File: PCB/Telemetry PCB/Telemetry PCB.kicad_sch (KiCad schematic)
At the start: 48 parts, among them IC1 E22-900M22S, J1 USB_C_Receptacle_USB2.0_16P, J2 Batt, J3 Serial Debug Header 1x4, J4 GPS, J5 Conn_01x04_Pin, SW1 SW_MEC_5E, SW2 SW_MEC_5E, U1 AP62200WU, U2 STM32F411CEUx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

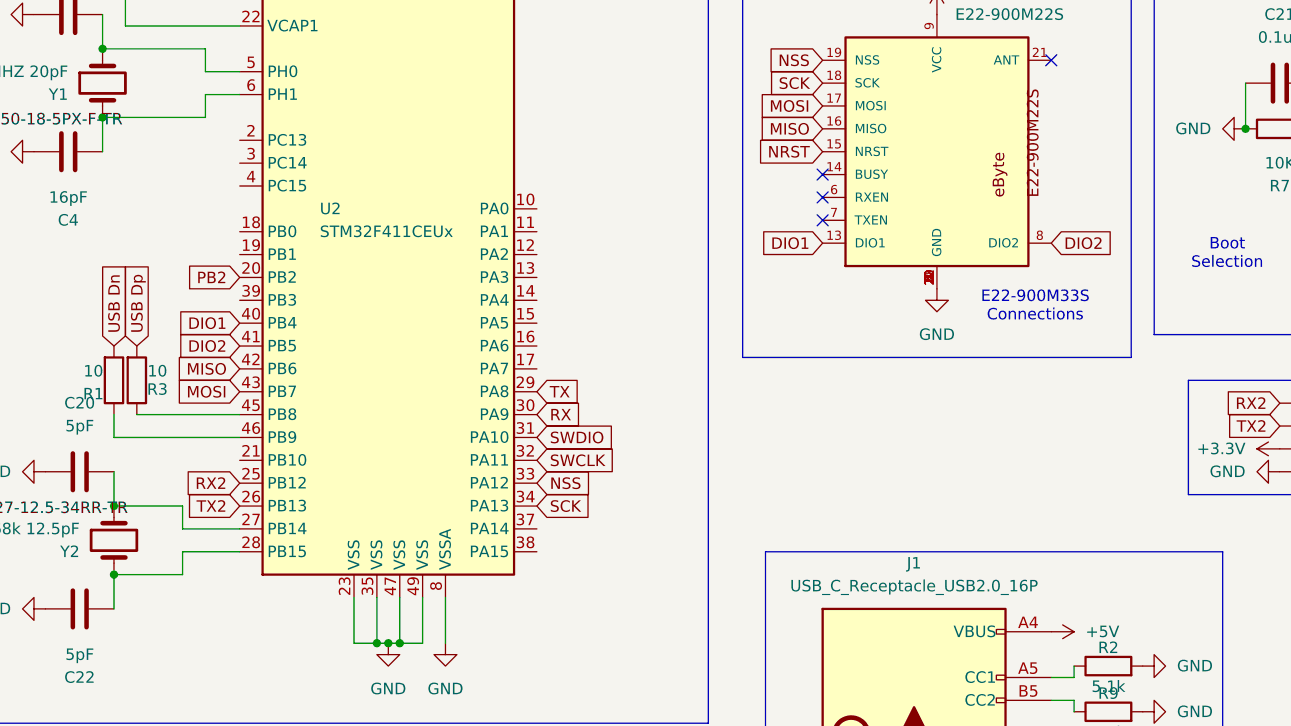
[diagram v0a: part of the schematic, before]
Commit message: Updated E22 connections
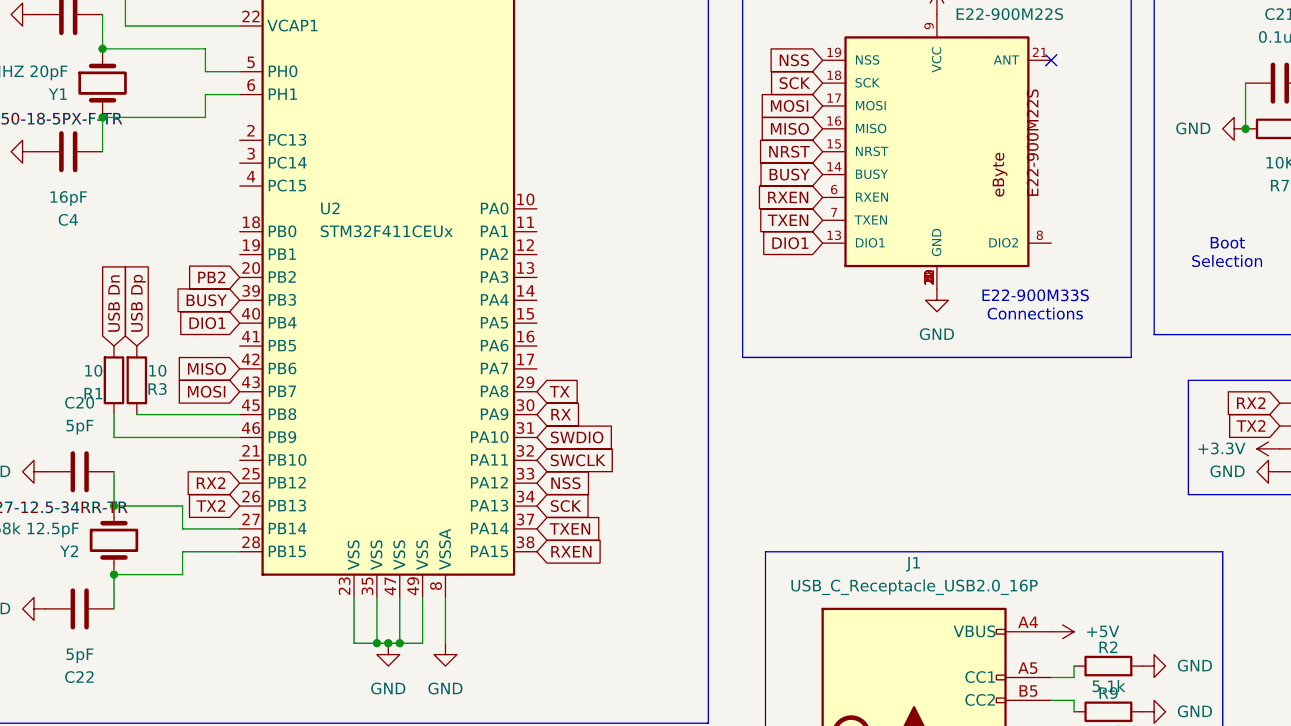
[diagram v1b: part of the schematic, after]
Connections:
- net BUSY: now reaches IC1.14 (BUSY)
- net BUSY: now also U2.39 (PB3)
- net RXEN: now reaches IC1.6 (RXEN)
- net RXEN: now also U2.38 (PA15)
- net TXEN: now reaches IC1.7 (TXEN)
- net TXEN: now also U2.37 (PA14)
- net DIO2: no longer names the net of IC1.8 (DIO2)
- net DIO2: no longer U2.41 (PB5)
- no-connect marks 8 -> 5
